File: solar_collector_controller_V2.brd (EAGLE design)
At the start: 49.5 x 50 mm, 28 parts, among them J2 GND +5V, T1 BC337, X1 22-23-2031, X2 22-23-2031, X3 22-23-2031, X5 22-23-2041

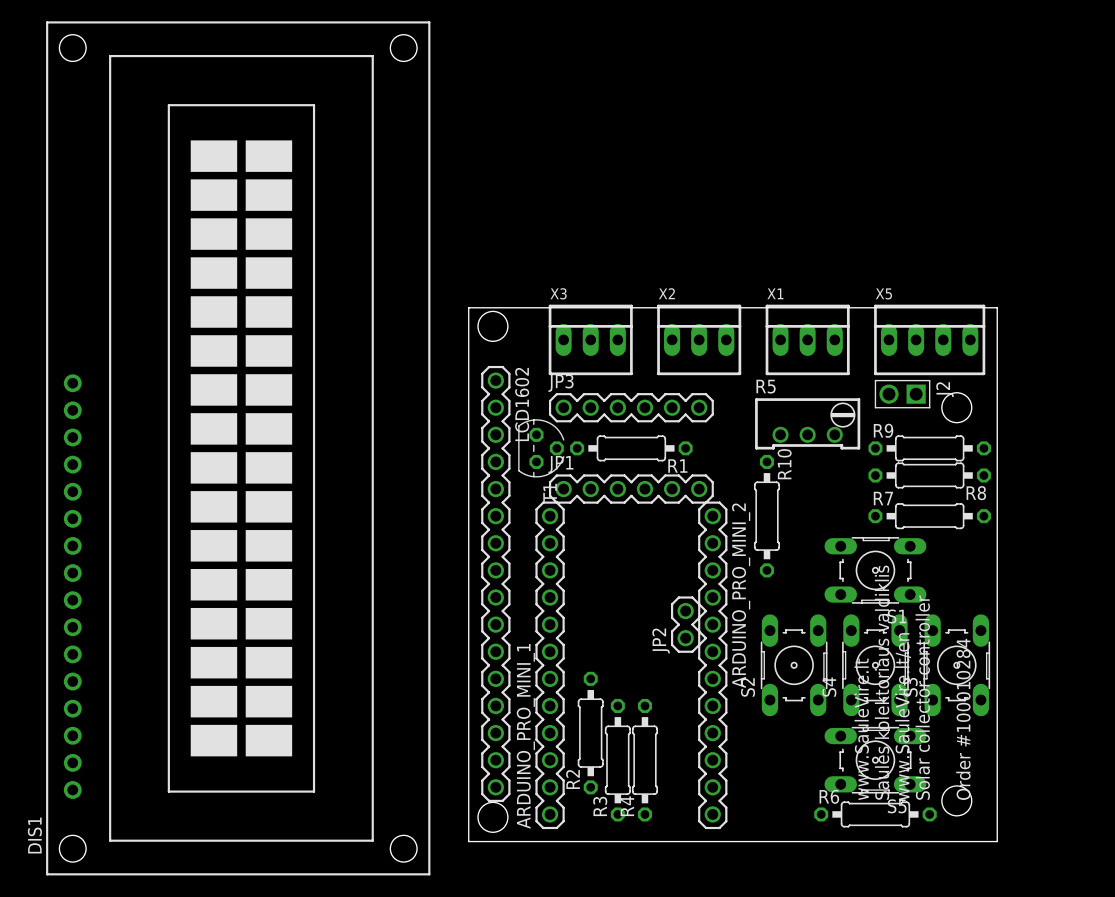
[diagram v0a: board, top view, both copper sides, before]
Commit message: pridetas tinklas, 3.3v
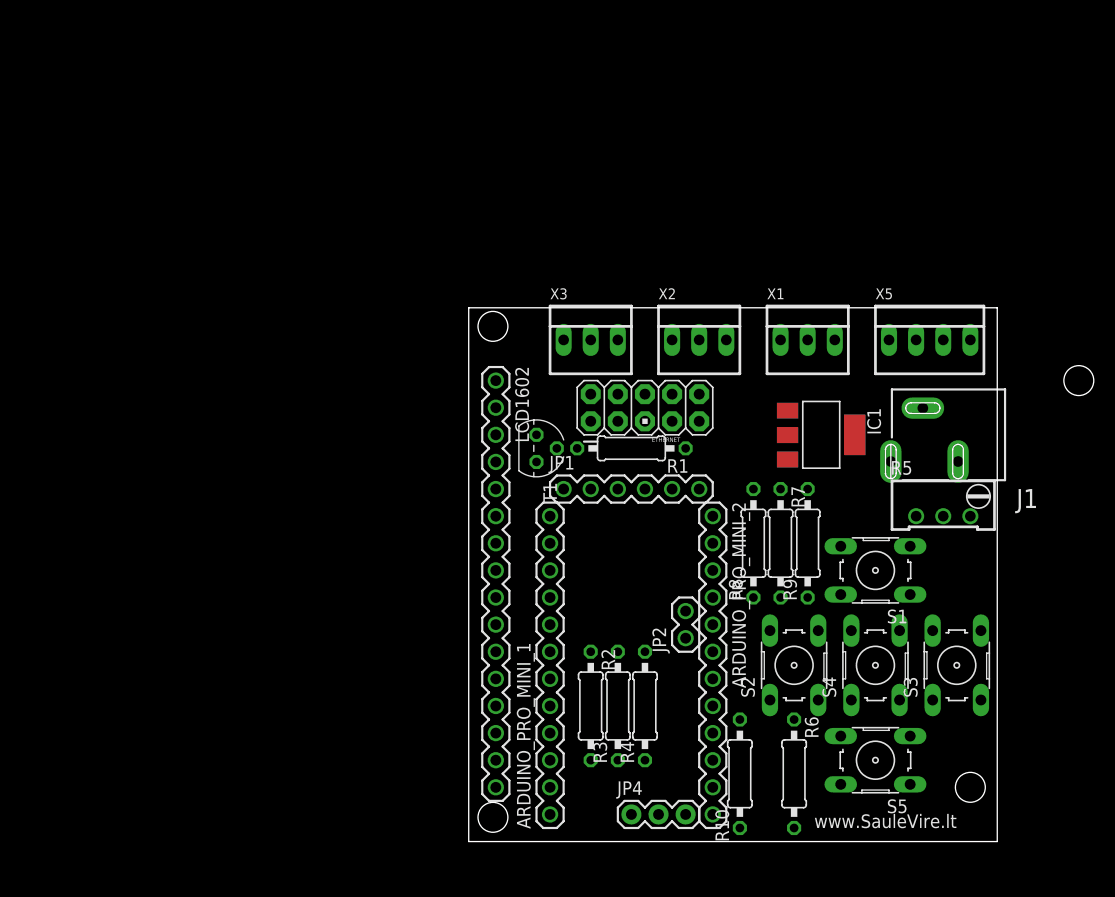
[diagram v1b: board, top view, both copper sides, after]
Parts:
- removed DIS1: TUXGR_16X2_R2, display-lcd:TUXGR_16X2_R2
- removed J2: GND +5V, Connector:2P-2.54
- removed JP3: vcc tx rx gnd, SparkFun:1X06
- added ETHERNET: M05X2PTH, SparkFun-Connectors:AVR_ICSP
- added IC1: REG1117, burr-brown:SOT223
- added J1: POWER_JACKSLT, SparkFun-Connectors:POWER_JACK_SLOT
- added JP4: (no value), SparkFun-Connectors:1X03
- moved R10 24.3 mm to (25.4, 6.35), turned to 270 degrees
- moved R8 17.7 mm to (26.7, 27.9), turned to 270 degrees
- moved R5 14.8 mm to (44.5, 31.8)
- moved R9 14.5 mm to (31.8, 27.9), turned to 270 degrees
- moved R7 14.2 mm to (29.2, 27.9), turned to 90 degrees
- moved R6 8.52 mm to (30.5, 6.35), turned to 90 degrees
- moved R3 5.08 mm to (14.0, 12.7)
- moved R4 5.08 mm to (16.5, 12.7)
- moved R2 2.54 mm to (11.4, 12.7), turned to 90 degrees
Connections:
- removed net N$13: R10.1, R9.2, S1.1, S1.2
- removed net N$3: R1.2
- removed net SCK: ARDUINO_PRO_MINI_2.9
- new net 3.3V: ETHERNET.9, IC1.2
- new net D13: ARDUINO_PRO_MINI_2.9, ETHERNET.6
- net A0: now also R10.1, R9.2, S1.1, S1.2
- net A4: now also R2.2, X1.2
- net A5: now also LCD1602.4
- net D10: now also R1.2; no longer R4.2, X3.2
- net D11: now also ETHERNET.5
- net D12: now also ETHERNET.4
- net D2: now also ETHERNET.2; no longer LCD1602.4
- net D8: now also ETHERNET.7; no longer R2.2, X1.2
- net GND: now also ETHERNET.10, IC1.1; no longer DIS1.1, J2.2, JP3.5
- net N$2: no longer LCD1602.2
- net RESET: now also ETHERNET.8
- net RXI: no longer JP3.3
- net TXO: no longer JP3.4
- net VCC: now also IC1.3, LCD1602.2; no longer DIS1.2, J2.1, JP3.2
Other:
- board text added: "www.SauleVire.lt"
- board text removed: "www.SauleVire.lt Saules kolektoriaus valdiklis www.SauleVire.lt/en Solar collector controller Order #100010284"
